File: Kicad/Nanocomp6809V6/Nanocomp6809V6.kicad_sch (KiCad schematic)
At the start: 77 parts, among them J1 TTL_USB_Serial_FT232R, J2 DB15_Female_HighDensity, J3 Conn_01x15_Male, SW1 R, SW10 0, SW11 3, SW12 2, SW13 D, SW14 C, SW15 B, SW16 A, SW17 1, SW18 4, SW19 7, SW2 F, SW20 G, SW21 CN, SW22 S, SW23 L, SW24 RST, SW25 AB, SW3 6, SW4 5, SW5 M, SW6 E, SW7 9, SW8 8, SW9 I, U1 MC6809, U10 74LS92, U11 MC6850, U12 74LS245, U13 74LS541BB, U14 74LS541BB, U15 74LS541BB, U16 74LS241BB, U17 74LS157BB, U18 74LS166BB, U19 74LS04, U2 ATF22LV10, U20 REN7134-Memory_RAM, U21 74LS163-74xx, U22 74LS10, U23 MC6845BB, U24 REN7134-Memory_RAM, U3 28C64B, U4 AS6C1008, U5 6821_BBPIN, U6 7_Segment_x_4_LED_Nanocomp_RH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, U7 ULN2803A, U8 74LS145, U9 7_Segment_x_4_LED_Nanocomp, Y1 4Mhz, Y2 MXO45HS-3C-3M6862, Y3 MXO45HS-3C-25M1750

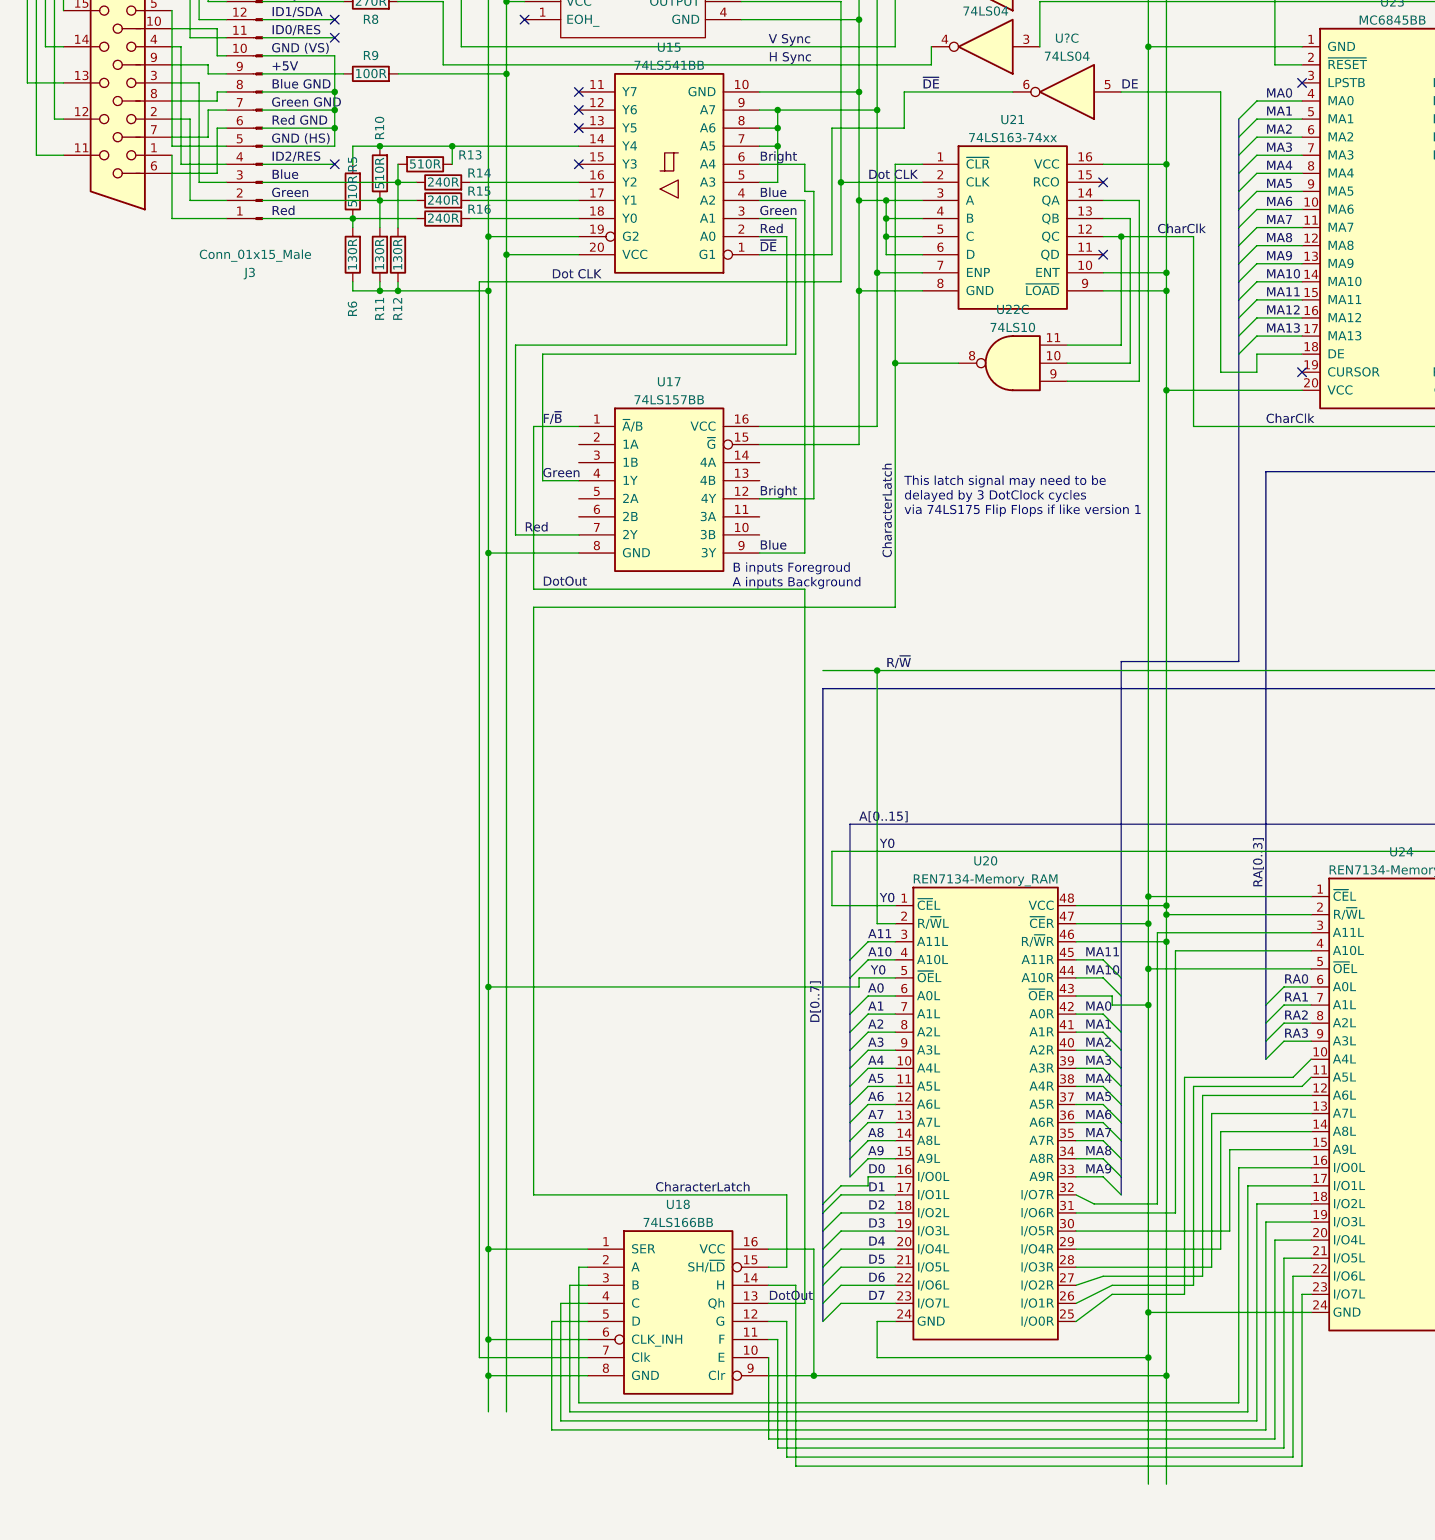
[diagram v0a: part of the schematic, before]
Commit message: Updated for Videos V04 & V05 Timing  & PLD
Updated with V6 and V7 Schematics with Timing enhancements then placement of 6 logic chips with 1 PLD/GAL
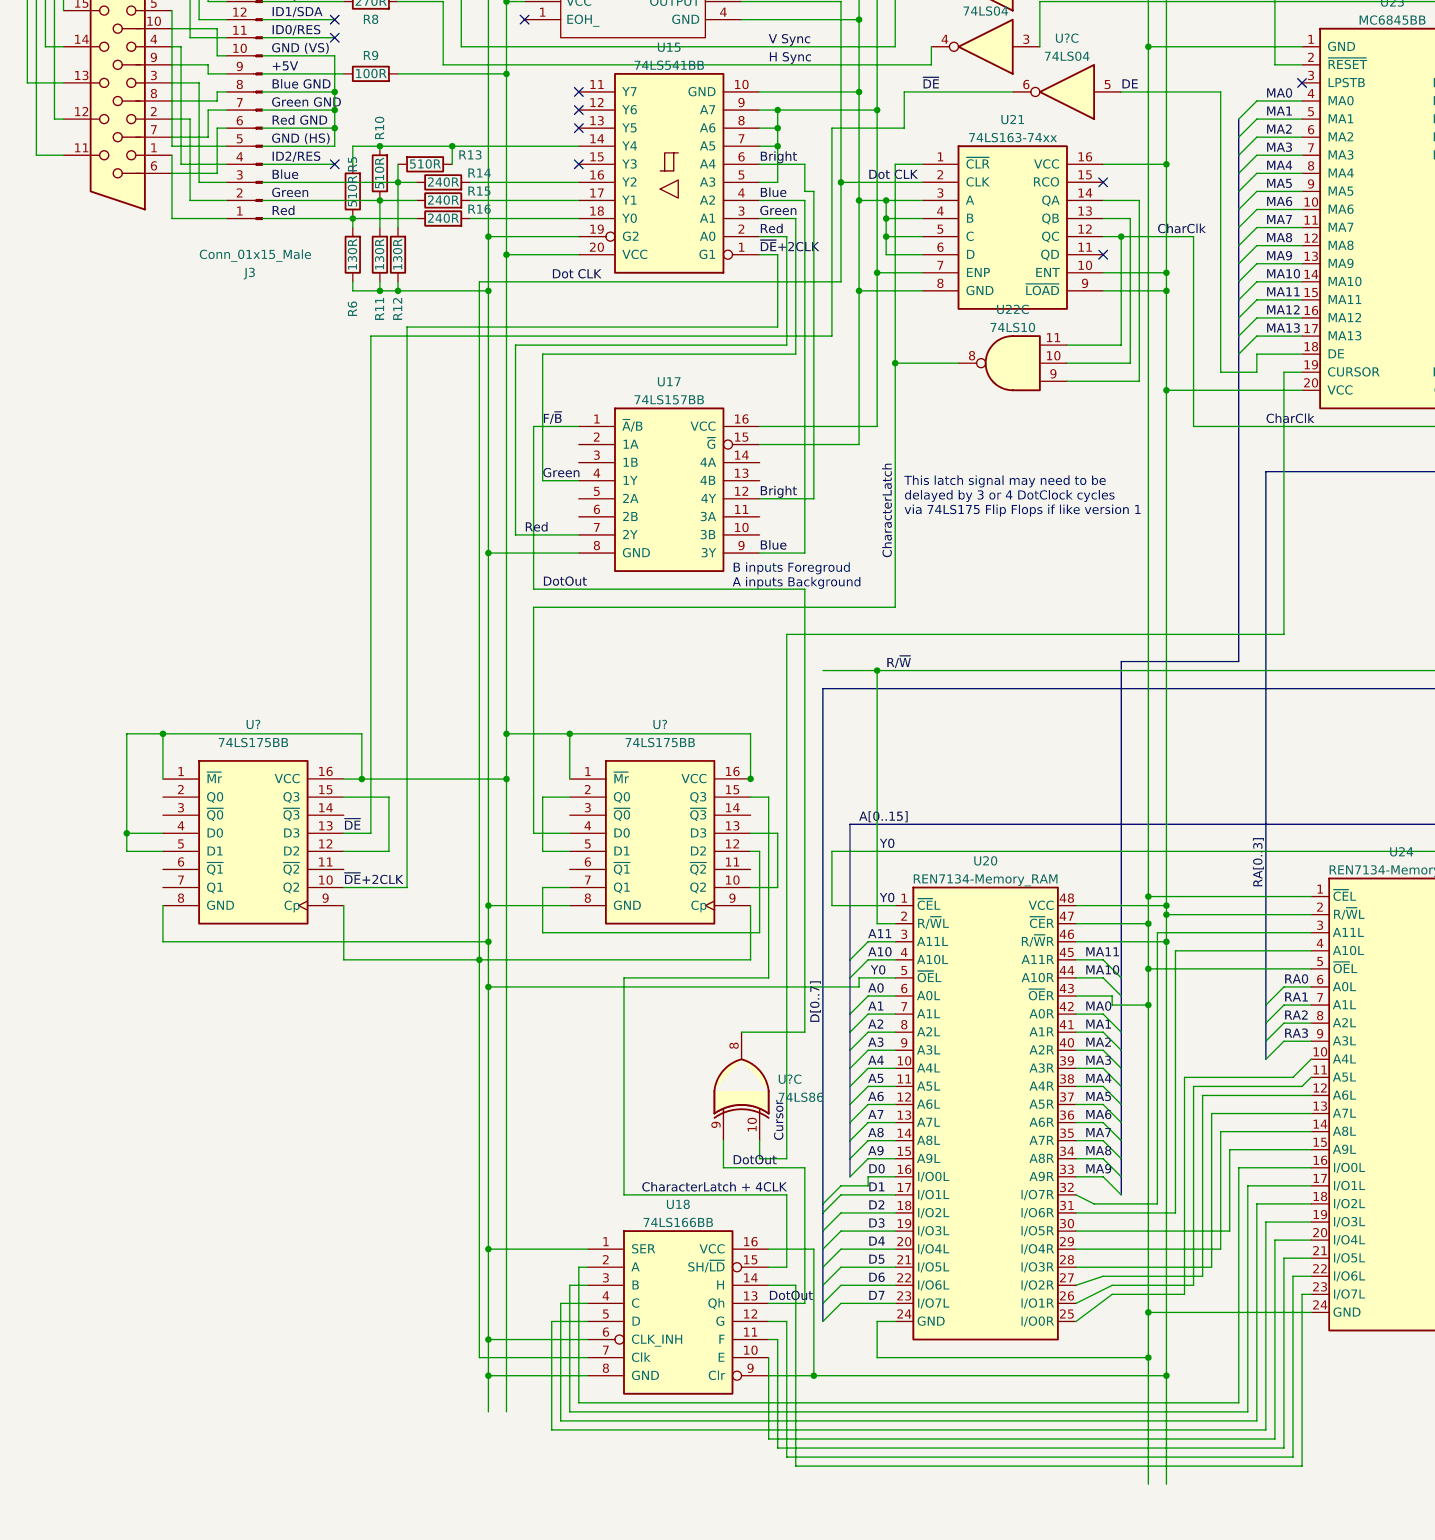
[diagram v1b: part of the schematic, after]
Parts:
- added U? (x2): 74LS175BB, symbol Breadboarding:74LS175BB
- added U?: 74LS86, symbol 74xx:74LS86
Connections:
- net 25.175MHz: now also U?.9 (Cp), U?.9 (Cp)
- net CharacterLatch: now also U?.4 (D0); no longer U18.15 (SH/~{LD})
- net DotOut: now also U?.8, U?.9
- net GND: now also U?.8 (GND), U?.8 (GND)
- net VCC: now also U?.1 (~{Mr}), U?.1 (~{Mr}), U?.16 (VCC), U?.4 (D0), U?.5 (D1)
- net ~{DE}: now also U?.13 (D3); no longer U15.1 (G1)
- net Cursor: now reaches U23.19 (CURSOR)
- net Cursor: now also U?.10
- new net: U?.12 (D2), U?.15 (Q3)
- new net: U?.10 (Q2), U?.13 (D3)
- new net: U?.12 (D2), U?.7 (Q1)
- new net: U?.2 (Q0), U?.5 (D1)
- new net CharacterLatch + 4CLK: U18.15 (SH/~{LD}), U?.15 (Q3)
- new net ~{DE}+2CLK: U15.1 (G1), U?.10 (Q2)
- no-connect marks 46 -> 45
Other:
- note added: "This latch signal may need to be delayed by 3 or 4 DotClock cycles via 74LS175 Flip Flops if like version 1"
- note removed: "This latch signal may need to be delayed by 3 DotClock cycles via 74LS175 Flip Flops if like version 1"
